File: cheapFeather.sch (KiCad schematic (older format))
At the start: 36 parts, among them J1 Conn_01x12, J2 Conn_01x16, J3 USB_B_Micro, J4 Conn_01x02, J5 Conn_01x02, Q1 BS170F, Q2 BS170F, Q3 BS170F, SW1 SW_Push, SW2 SW_Push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

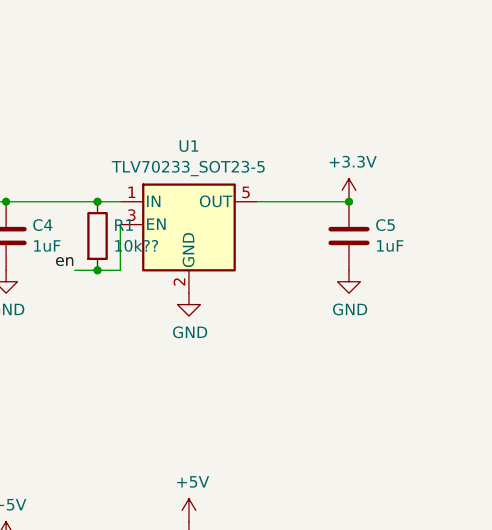
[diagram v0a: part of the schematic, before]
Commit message: Changed cap. values
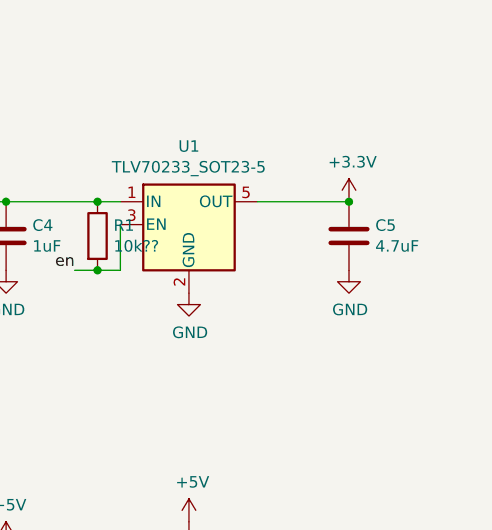
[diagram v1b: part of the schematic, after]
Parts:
- C5: value 1uF -> 4.7uF
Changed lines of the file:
@@
 P 9600 1400
 F 0 "C5" H 9715 1446 50  0000 L CNN
-F 1 "1uF" H 9715 1355 50  0000 L CNN
+F 1 "4.7uF" H 9715 1355 50  0000 L CNN
 F 2 "Capacitor_SMD:C_0805_2012Metric" H 9638 1250 50  0001 C CNN
 F 3 "~" H 9600 1400 50  0001 C CNN
